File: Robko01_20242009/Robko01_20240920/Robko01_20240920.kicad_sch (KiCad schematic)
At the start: 73 parts, among them J1 Conn_01x04_Pin, J10 Motors, J11 Motors, J12 Conn_01x04_Pin, J13 Conn_01x02_Pin, J14 Conn_01x04_Pin, J15 Conn_01x02_Pin, J16 Conn_01x04_Pin, J17 Conn_01x02_Male, J18 Conn_01x02_Male, J19 Conn_01x02_Male, J2 Conn_01x02_Pin, J20 Conn_01x02_Male, J21 Conn_01x19_Pin, J22 Conn_01x19_Pin, J23 Conn_01x06_Pin, J24 Conn_01x04_Pin, J25 Conn_01x04_Pin, J26 Conn_01x04_Pin, J27 Conn_01x06_Pin, J28 Conn_01x02_Male, J29 Conn_01x07_Pin, J3 Conn_01x02_Pin, J30 Conn_01x02_Male, J4 Conn_01x04_Pin, J5 Conn_01x02_Pin, J6 Conn_01x04_Pin, J7 Conn_01x02_Male, J8 Conn_01x02_Pin, J9 Motors, K2 G5V-2, SW1 SW_DIP_x04, SW2 SW_DIP_x04, SW3 SW_DIP_x04, SW4 SW_DIP_x04, SW5 SW_DIP_x04, SW7 SW_DIP_x04, U1 LM7805_TO220, U2 PC817

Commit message: Add UEXT
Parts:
- removed J23, J27: Conn_01x06_Pin, Connector_PinHeader_2.54mm:PinHeader_1x06_P2.54mm_Horizontal, symbol Connector:Conn_01x06_Pin
- removed J24, J25, J26: Conn_01x04_Pin, Connector_PinHeader_2.54mm:PinHeader_1x04_P2.54mm_Horizontal, symbol Connector:Conn_01x04_Pin
- added J23, J31: Conn_02x05_Odd_Even, Connector_IDC:IDC-Header_2x05_P2.54mm_Horizontal, symbol Connector_Generic:Conn_02x05_Odd_Even
- added JP10, JP12, JP13, JP7: SolderJumper_2_Open, Jumper:SolderJumper-2_P1.3mm_Open_RoundedPad1.0x1.5mm, symbol Jumper:SolderJumper_2_Open
- added JP11, JP14, JP8, JP9: SolderJumper_2_Bridged, Jumper:SolderJumper-2_P1.3mm_Bridged2Bar_RoundedPad1.0x1.5mm, symbol Jumper:SolderJumper_2_Bridged
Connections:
- net +3.3V: now also J23.1 (Pin_1), J31.1 (Pin_1)
- net GND: now also J20.2 (Pin_2), J23.2 (Pin_2), J31.2 (Pin_2); no longer J20.1 (Pin_1)
- net MCU_RESET: now also J20.1 (Pin_1); no longer J20.2 (Pin_2)
- net RX0: now also JP10.2 (B), JP9.1 (A)
- net SCL: now also J23.5 (Pin_5), J31.5 (Pin_5)
- net SDA: now also J23.6 (Pin_6), J31.6 (Pin_6)
- net TX0: now also JP7.1 (A), JP8.2 (B)
- net VSPI_MISO: now also JP13.2 (B), JP14.1 (A)
- net VSPI_MOSI: now also JP11.2 (B), JP12.1 (A)
- net VSPI_SCK: now also J23.9 (Pin_9), J31.9 (Pin_9)
- net VSPI_SS: now also J23.10 (Pin_10), J31.10 (Pin_10)
- new net: J23.3 (Pin_3), J31.3 (Pin_3), JP10.1 (A), JP8.1 (A)
- new net: J23.4 (Pin_4), J31.4 (Pin_4), JP7.2 (B), JP9.2 (B)
- new net: J23.7 (Pin_7), J31.7 (Pin_7), JP12.2 (B), JP14.2 (B)
- new net: J23.8 (Pin_8), J31.8 (Pin_8), JP11.1 (A), JP13.1 (A)
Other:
- note added: "UEXT"
- note removed: "I2C"
- note removed: "SPI"
- note removed: "UART"
- moved on the sheet: J17, J18, J20, J29, J30, R2, RN1, U2

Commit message: Change jumpers for UEXT
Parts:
- removed JP10, JP12, JP13, JP7: SolderJumper_2_Open, Jumper:SolderJumper-2_P1.3mm_Open_RoundedPad1.0x1.5mm, symbol Jumper:SolderJumper_2_Open
- removed JP11, JP14, JP8, JP9: SolderJumper_2_Bridged, Jumper:SolderJumper-2_P1.3mm_Bridged2Bar_RoundedPad1.0x1.5mm, symbol Jumper:SolderJumper_2_Bridged
- added JP15, JP16, JP7, JP8: Jumper_3_Bridged12, Jumper:SolderJumper-3_P1.3mm_Bridged2Bar12_Pad1.0x1.5mm, symbol Jumper:Jumper_3_Bridged12
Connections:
- net RX0: now also JP16.2 (C)
- net TX0: now also JP15.2 (C)
- net VSPI_MISO: now also JP7.2 (C)
- net VSPI_MOSI: now also JP8.2 (C)
- net at J23.3 (Pin_3), J31.3 (Pin_3): now also JP15.1 (A), JP16.3 (B)
- net at J23.4 (Pin_4), J31.4 (Pin_4): now also JP15.3 (B), JP16.1 (A)
- net at J23.7 (Pin_7), J31.7 (Pin_7): now also JP7.1 (A), JP8.3 (B)
- net at J23.8 (Pin_8), J31.8 (Pin_8): now also JP7.3 (B), JP8.1 (A)
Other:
- moved on the sheet: J23, J31

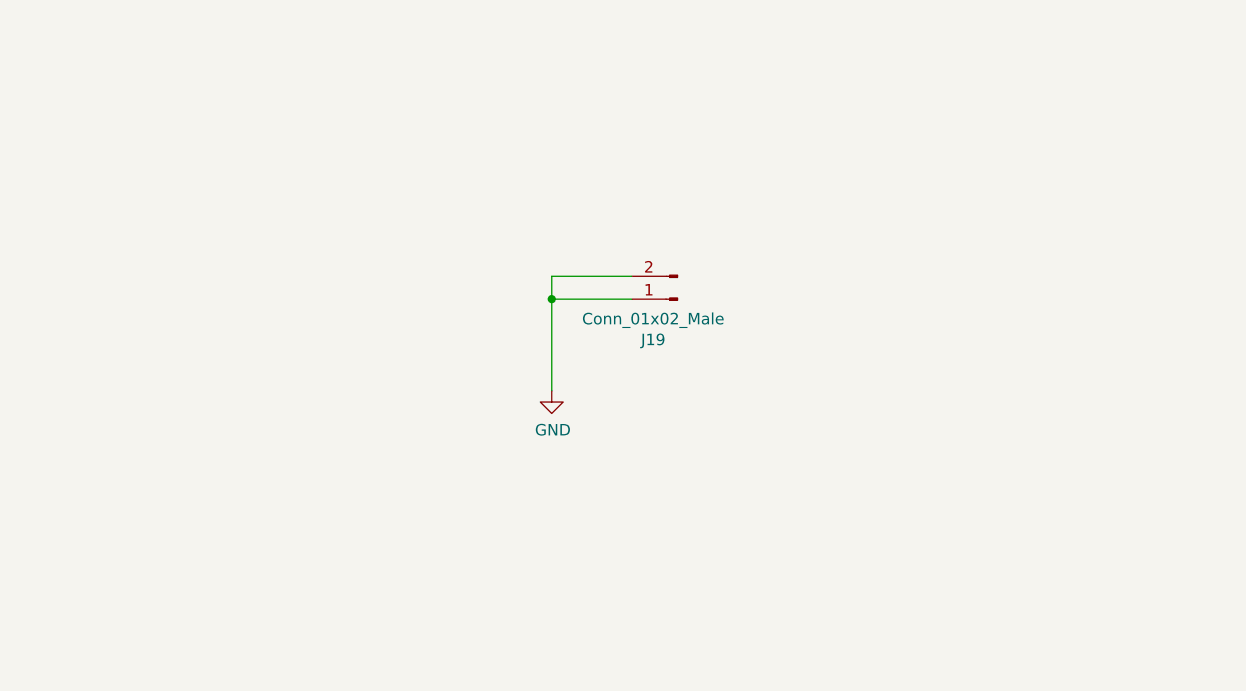
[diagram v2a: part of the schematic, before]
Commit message: Add USB
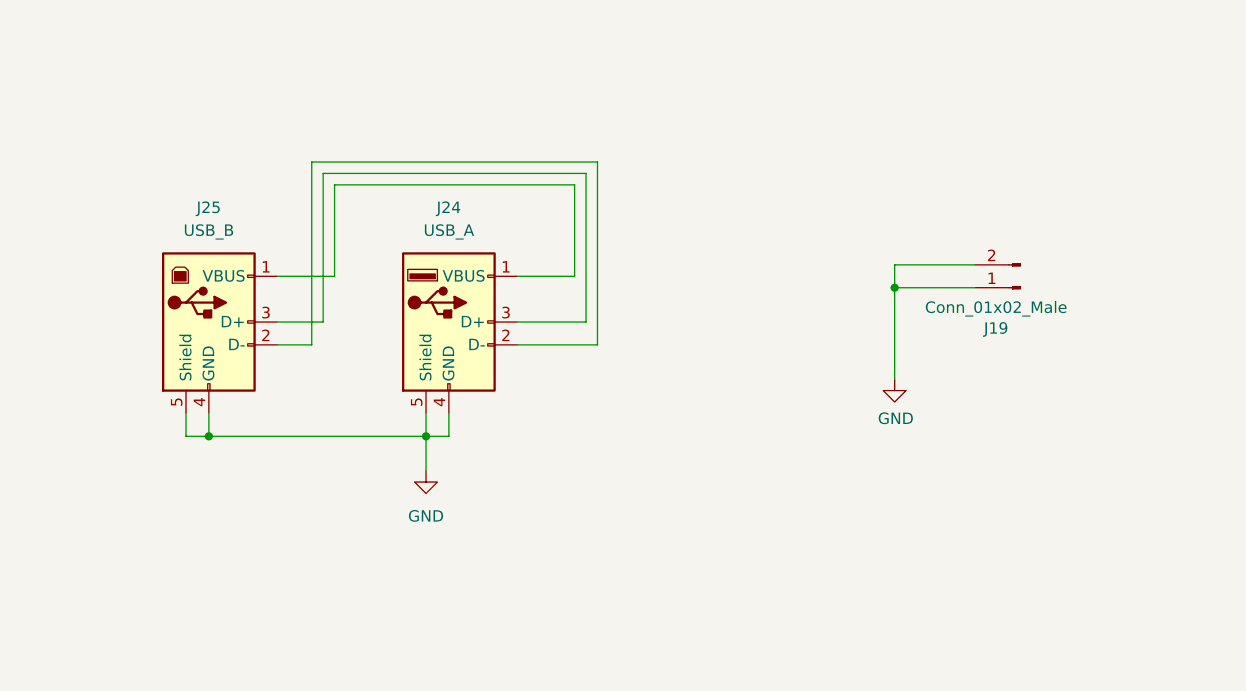
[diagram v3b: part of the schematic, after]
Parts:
- added J24: USB_A, Connector_USB:USB_A_Molex_67643_Horizontal, symbol Connector:USB_A
- added J25: USB_B, Connector_USB:USB_B_Lumberg_2411_02_Horizontal, symbol Connector:USB_B
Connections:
- net GND: now also J24.4 (GND), J24.5 (Shield), J25.4 (GND), J25.5 (Shield)
- new net: J24.1 (VBUS), J25.1 (VBUS)
- new net: J24.2 (D-), J25.2 (D-)
- new net: J24.3 (D+), J25.3 (D+)
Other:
- moved on the sheet: J19

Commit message: Change E-Stop connector, add default jumper to power supply of the stepper drivers, wireup limit switch of the gripper, rewire E-Stop sensor
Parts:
- removed J18, J20, J30: Conn_01x02_Male, Connector_PinHeader_2.54mm:PinHeader_1x02_P2.54mm_Horizontal, symbol Robko01-rescue:Conn_01x02_Male-Connector
- removed J29: Conn_01x07_Pin, Connector_PinHeader_2.54mm:PinHeader_1x07_P2.54mm_Horizontal, symbol Connector:Conn_01x07_Pin
- removed RN1: R_Network04, Resistor_THT:R_Array_SIP5, symbol Device:R_Network04
- added J18: Conn_01x06_Pin, Connector_PinHeader_2.54mm:PinHeader_1x06_P2.54mm_Horizontal, symbol Connector:Conn_01x06_Pin
- added JP10, JP11, JP12, JP13, JP14, JP9: SolderJumper_2_Bridged, Jumper:SolderJumper-2_P1.3mm_Bridged2Bar_RoundedPad1.0x1.5mm, symbol Jumper:SolderJumper_2_Bridged
- added RN1: R_Network05, Resistor_THT:R_Array_SIP6, symbol Device:R_Network05
- added SW6: RESET, Button_Switch_THT:SW_Tactile_SPST_Angled_PTS645Vx39-2LFS, symbol Switch:SW_Push
- C1, C2: value 100nF -> 100n; footprint Capacitor_THT:C_Disc_D7.5mm_W2.5mm_P5.00mm -> Capacitor_THT:C_Disc_D7.0mm_W2.5mm_P5.00mm
- D3: value LED -> LED 3mm Green
- D4: value LED -> LED 3mm Red
- J17: footprint Connector_Phoenix_MSTB:PhoenixContact_MSTBA_2,5_2-G-5,08_1x02_P5.08mm_Horizontal -> Connector_Phoenix_MC:PhoenixContact_MC_1,5_2-G-3.5_1x02_P3.50mm_Horizontal
- J19: value Conn_01x02_Male -> TP-GND
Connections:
- net GPIO15 is gone; now on net E-STOP: J22.16 (Pin_16)
- net GRIPPER_1 is gone; now on net GND: J9.13 (Pin_13)
- net GRIPPER_2 is gone; now on net GPIO35: J11.13 (Pin_13)
- net +3.3V: now also RN1.1 (common)
- net +5V: now also J18.1 (Pin_1)
- net GND: now also J18.2 (Pin_2), SW6.2
- net GPIO35: no longer J21.6 (Pin_6)
- net MCU_RESET: now also SW6.1
- net VCC: no longer J13.1 (Pin_1), J15.1 (Pin_1), J17.2 (Pin_2), J2.1 (Pin_1), J3.1 (Pin_1), J5.1 (Pin_1), J8.1 (Pin_1), R2.1
- net at A2.8 (VMOT), C5.1, C6.1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: now also JP10.2 (B)
- net at A6.8 (VMOT), C13.1, C14.1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: now also JP14.2 (B)
- net at A5.8 (VMOT), C11.1, C12.1: now also J8.2 (Pin_2), JP13.2 (B); no longer J13.2 (Pin_2)
- net at A4.8 (VMOT), C10.1, C9.1: now also J13.2 (Pin_2), JP12.2 (B); no longer J8.2 (Pin_2)
- net at A1.4 (1A), J1.3 (Pin_3): no longer J11.3 (Pin_3)
- net at A1.8 (VMOT), C3.1, C4.1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: now also JP9.2 (B)
- net at A3.8 (VMOT), C7.1, C8.1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: now also JP11.2 (B)
- net E-STOP: now reaches U2.4
- net E-STOP: now also RN1.6 (R5)
- net GPIO34 renamed M1-Limit
- net M1-Limit: now also J18.4 (Pin_4), RN1.4 (R3)
- net GPIO36 renamed M3-Limit
- net M3-Limit: now also J18.6 (Pin_6), RN1.2 (R1)
- net GPIO39 renamed M2-Limit
- net M2-Limit: now also J18.5 (Pin_5), RN1.3 (R2)
- new net M6-Limit: J18.3 (Pin_3), J21.6 (Pin_6), RN1.5 (R4)
- new net MC_POWER: J13.1 (Pin_1), J15.1 (Pin_1), J17.2 (Pin_2), J2.1 (Pin_1), J3.1 (Pin_1), J5.1 (Pin_1), J8.1 (Pin_1), JP10.1 (A), JP11.1 (A), JP12.1 (A), JP13.1 (A), JP14.1 (A), JP9.1 (A), R2.1
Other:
- moved on the sheet: J15, J17, J2, J5, R2, U2
